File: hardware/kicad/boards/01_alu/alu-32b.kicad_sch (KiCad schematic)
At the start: 34 parts, among them J1 Conn_02x16_Odd_Even, J2 Conn_02x16_Odd_Even, J3 Conn_02x04_Odd_Even, J4 Conn_02x16_Odd_Even, J5 Conn_02x16_Counter_Clockwise, SW1 SW_DIP_x08, SW10 SW_DIP_x08, SW11 SW_DIP_x08, SW12 SW_DIP_x08, SW13 SW_DIP_x08, SW2 SW_DIP_x08, SW3 SW_DIP_x08, SW4 SW_DIP_x08, SW5 SW_DIP_x08, SW6 SW_DIP_x08, SW7 SW_SPDT, SW8 SW_DIP_x08, SW9 SW_DIP_x08

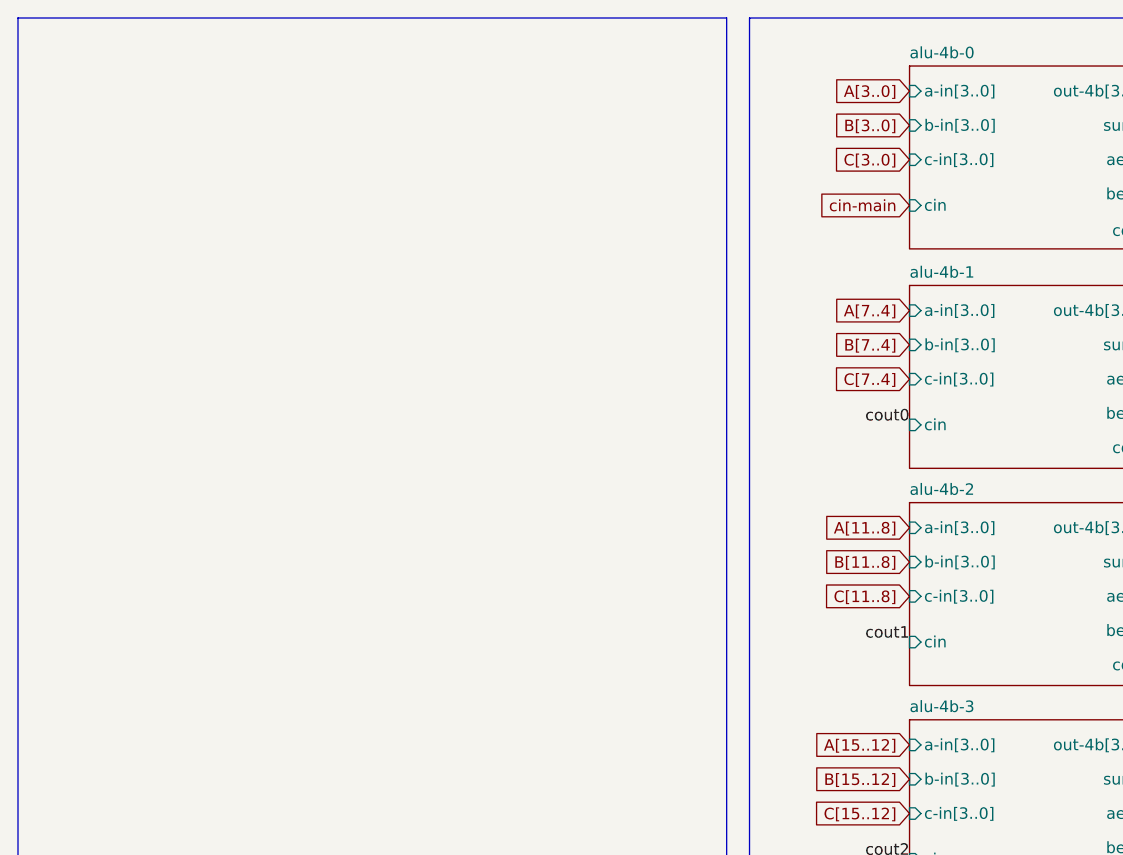
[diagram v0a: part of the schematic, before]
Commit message: feat: added 8to1 mux for cin variety; routed major bus on RHS cells; updated main.dig with cin mux
Updated alu-control with correct global labels for cin-sel[2..0]
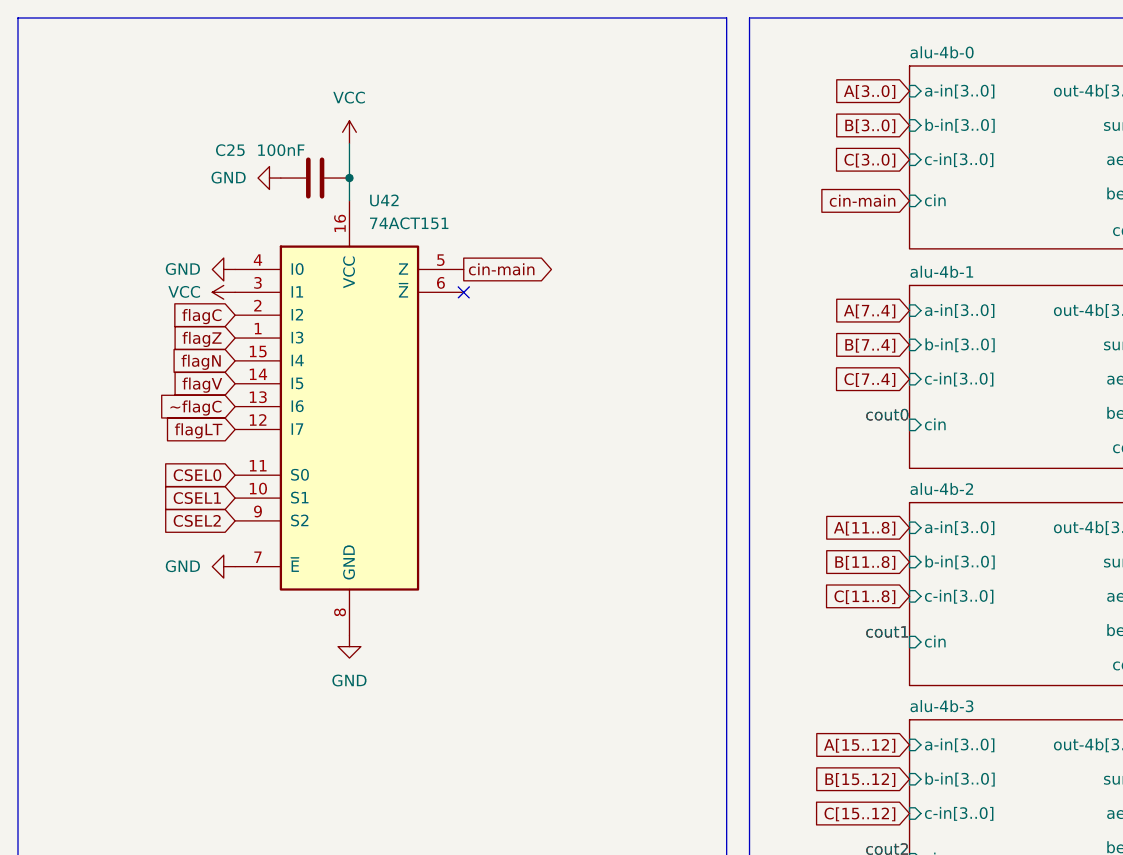
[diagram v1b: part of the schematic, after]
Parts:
- added C25: 100nF, Capacitor_SMD:C_0603_1608Metric, symbol Device:C
- added U42: 74ACT151, Package_SO:SOIC-16_3.9x9.9mm_P1.27mm, symbol 74xx:74LS151
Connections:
- net GND: now also C25.1, U42.4 (I0), U42.7 (~{E}), U42.8 (GND)
- net VCC: now also C25.2, U42.16 (VCC), U42.3 (I1)
- net cin-main: now also U42.5 (Z)
- new net CSEL0: U42.11 (S0)
- new net CSEL1: U42.10 (S1)
- new net CSEL2: U42.9 (S2)
- new net flagC: U42.2 (I2)
- new net flagLT: U42.12 (I7)
- new net flagN: U42.15 (I4)
- new net flagV: U42.14 (I5)
- new net flagZ: U42.1 (I3)
- new net ~flagC: U42.13 (I6)
- no-connect marks 22 -> 23

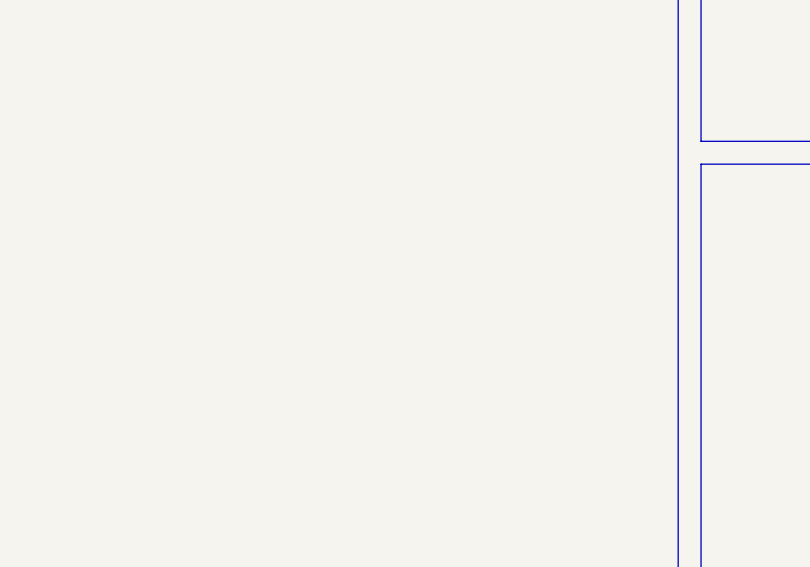
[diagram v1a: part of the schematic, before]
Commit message: feat: laid the main bus; adding control unit and display segments
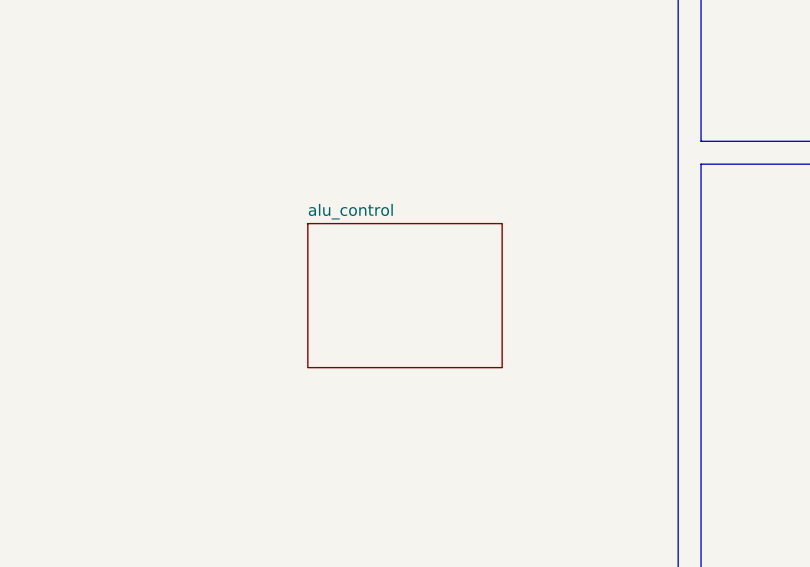
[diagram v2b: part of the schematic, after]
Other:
- added sheet alu_control (alu-control.kicad_sch)
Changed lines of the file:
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@@
+	)
+	(sheet
+		(at 228.092 278.384)
+		(size 21.59 16.002)
+		(exclude_from_sim no)
+		(in_bom yes)
+		(on_board yes)
+		(dnp no)
+		(fields_autoplaced yes)
+		(stroke
+			(width 0.1524)
+			(type solid)
+		)
+		(fill
+			(color 0 0 0 0)
+		)
+		(property "Sheetname" "alu_control"
+			(at 228.092 277.6724 0)
+			(show_name no)
+			(do_not_autoplace no)
+			(effects
+				(font
+					(size 1.27 1.27)
+				)
+				(justify left bottom)
+			)
+		)
+		(property "Sheetfile" "alu-control.kicad_sch"
+			(at 228.092 294.9706 0)
+			(hide yes)
+			(show_name no)
+			(do_not_autoplace no)
+			(effects
+				(font
+					(size 1.27 1.27)
+				)
+				(justify left top)
+			)
+		)
+		(instances
+			(project "alu-32b"
+				(path "/ddad1417-0afc-402d-a021-92fc87ddd78a"
+					(page "4")
+				)
+			)
+		)
 	)
 	(sheet
